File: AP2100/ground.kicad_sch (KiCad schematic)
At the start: 33 parts, among them U21 EMMC04G-M627-A01, U7 LS1043ASE7KQB-Layerscape

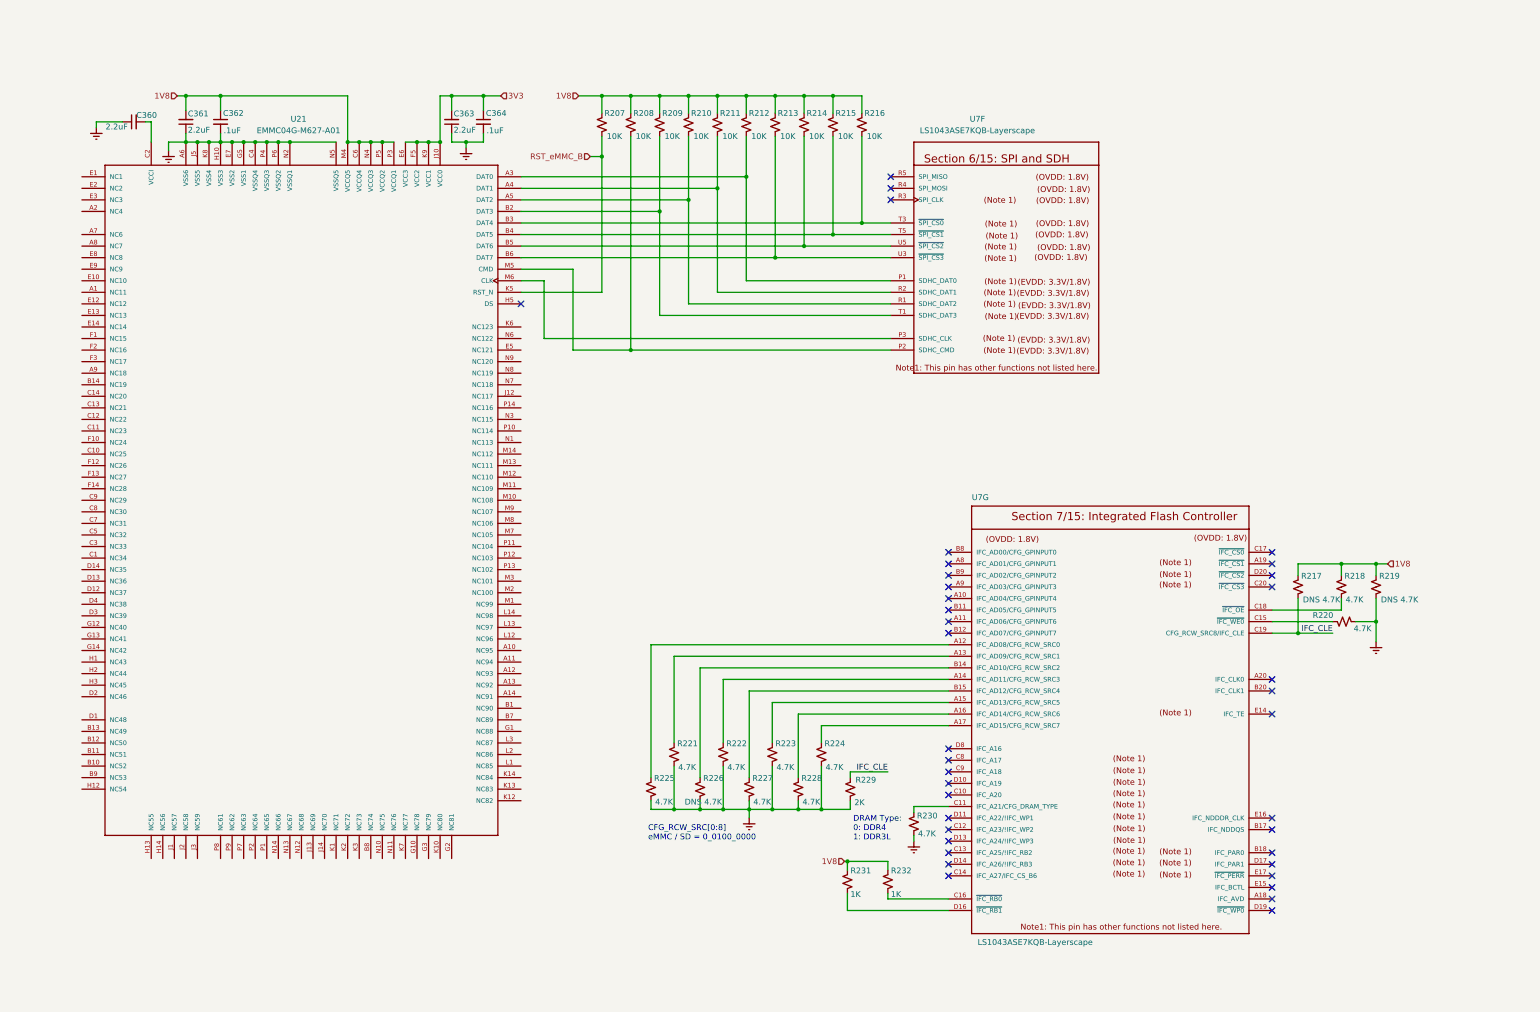
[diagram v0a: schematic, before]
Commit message: Review / cleanup footprints, etc
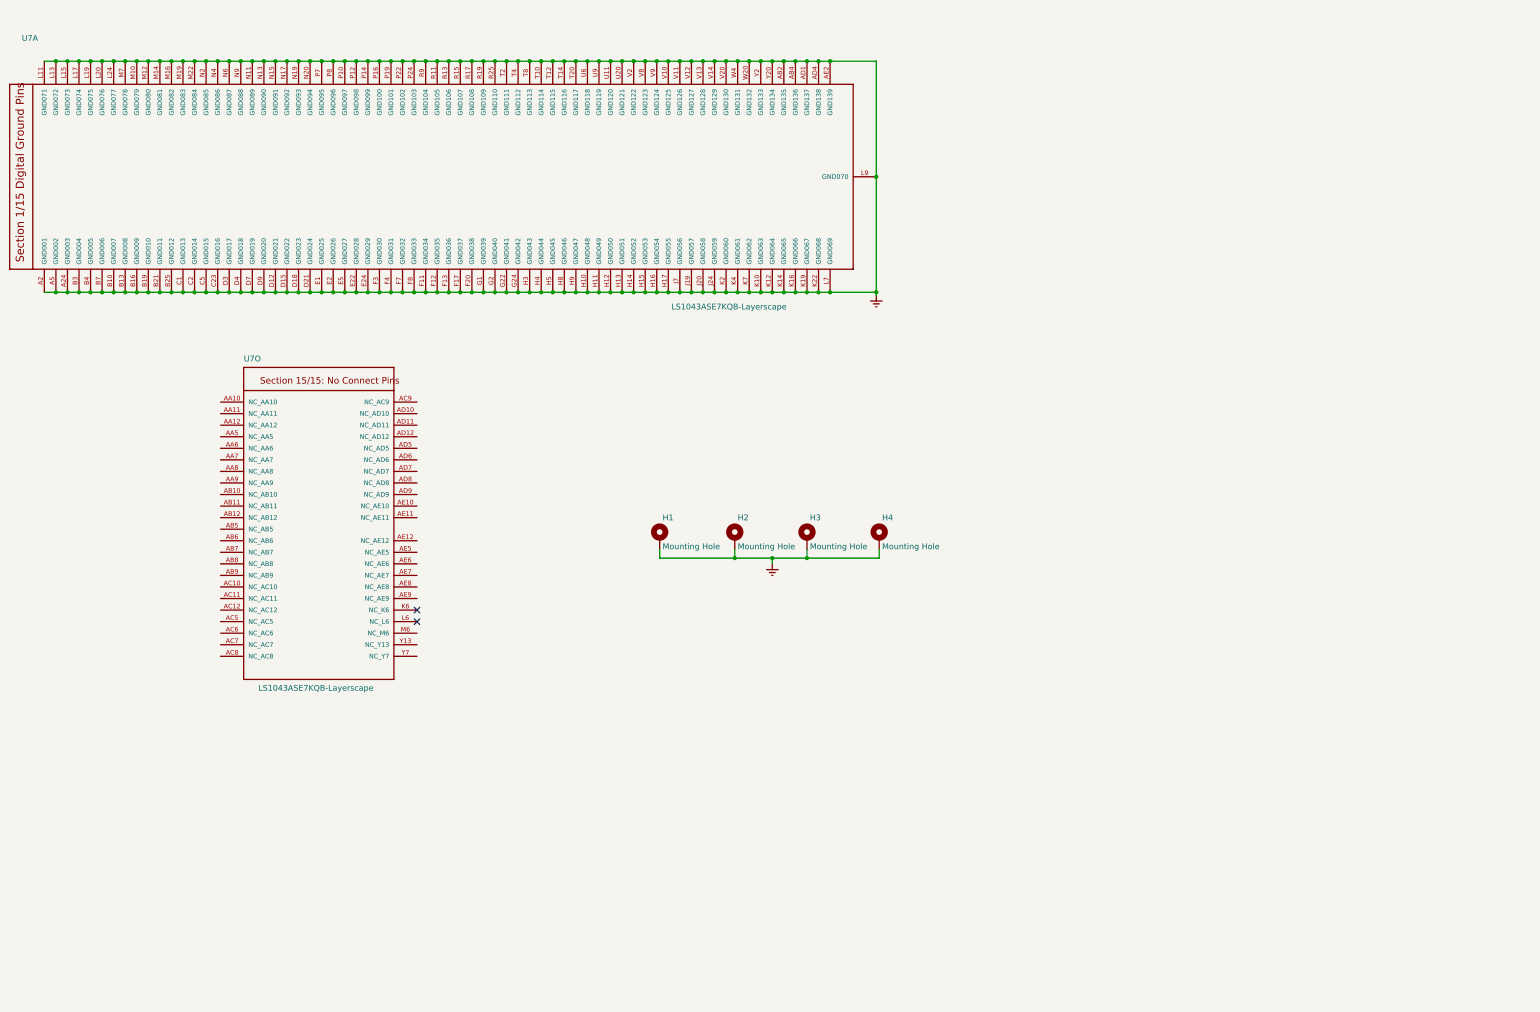
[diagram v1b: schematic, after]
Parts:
- removed C360, C361, C363: 2.2uF, Capacitor_SMD:C_0603_1608Metric, symbol Device:C_Small
- removed C362, C364: .1uF, Capacitor_SMD:C_0402_1005Metric, symbol Device:C_Small
- removed R207, R208, R209, R210, R211, R212, R213, R214, R215, R216: 10K, Resistor_SMD:R_0402_1005Metric, symbol Device:R_Small_US
- removed R217, R219, R226: DNS 4.7K, Resistor_SMD:R_0402_1005Metric, symbol Device:R_Small_US
- removed R218, R220, R221, R222, R223, R224, R225, R227, R228, R230: 4.7K, Resistor_SMD:R_0402_1005Metric, symbol Device:R_Small_US
- removed R229: 2K, Resistor_SMD:R_0402_1005Metric, symbol Device:R_Small_US
- removed R231, R232: 1K, Resistor_SMD:R_0402_1005Metric, symbol Device:R_Small_US
- removed U21: EMMC04G-M627-A01, LIB_EMMC04G-M627:BGA153N50P14X14_1300X1150X100N, symbol EMMC04G-M627-A01:EMMC04G-M627-A01
- removed U7: LS1043ASE7KQB-Layerscape, PLS1043ASE7QQA:BGA621C80P25X25_2100X2100X192N, symbol AP2100-rescue:LS1043ASE7KQB-Layerscape
- added H1, H2, H3, H4: Mounting Hole, MountingHole:MountingHole_2.5mm_Pad_TopBottom, symbol Mechanical:MountingHole_Pad
- added U7: LS1043ASE7KQB-Layerscape, PLS1043ASE7QQA:BGA621C80P25X25_2100X2100X192N, symbol AP2100-rescue:LS1043ASE7KQB-Layerscape
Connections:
- net GND: now also H1.1, H2.1, H3.1, H4.1, U7.A2 (GND001), U7.A24 (GND003), U7.A5 (GND002), U7.AB2 (GND135), U7.AB4 (GND136), U7.AD1 (GND137), U7.AD4 (GND138), U7.AE2 (GND139), U7.B10 (GND007), U7.B13 (GND008), U7.B16 (GND009), U7.B19 (GND010), U7.B21 (GND011), U7.B25 (GND012), U7.B3 (GND004), U7.B4 (GND005), U7.B7 (GND006), U7.C1 (GND013), U7.C2 (GND014), U7.C23 (GND016), U7.C5 (GND015), U7.D12 (GND021), U7.D15 (GND022), U7.D18 (GND023), U7.D21 (GND024), U7.D3 (GND017), U7.D4 (GND018), U7.D7 (GND019), U7.D9 (GND020), U7.E1 (GND025), U7.E2 (GND026), U7.E22 (GND028), U7.E24 (GND029), U7.E5 (GND027), U7.F11 (GND034), U7.F12 (GND035), U7.F13 (GND036), U7.F17 (GND037), U7.F20 (GND038), U7.F3 (GND030), U7.F4 (GND031), U7.F7 (GND032), U7.F8 (GND033), U7.G1 (GND039), U7.G2 (GND040), U7.G22 (GND041), U7.G24 (GND042), U7.H10 (GND048), U7.H11 (GND049), U7.H12 (GND050), U7.H13 (GND051), U7.H14 (GND052), U7.H15 (GND053), U7.H16 (GND054), U7.H17 (GND055), U7.H3 (GND043), U7.H4 (GND044), U7.H5 (GND045), U7.H8 (GND046), U7.H9 (GND047), U7.J19 (GND057), U7.J20 (GND058), U7.J24 (GND059), U7.J7 (GND056), U7.K10 (GND063), U7.K12 (GND064), U7.K14 (GND065), U7.K16 (GND066), U7.K19 (GND067), U7.K2 (GND060), U7.K22 (GND068), U7.K4 (GND061), U7.K7 (GND062), U7.L11 (GND071), U7.L13 (GND072), U7.L15 (GND073), U7.L17 (GND074), U7.L19 (GND075), U7.L20 (GND076), U7.L24 (GND077), U7.L7 (GND069), U7.L9 (GND070), U7.M10 (GND079), U7.M12 (GND080), U7.M14 (GND081), U7.M16 (GND082), U7.M19 (GND083), U7.M22 (GND084), U7.M7 (GND078), U7.N11 (GND089), U7.N13 (GND090), U7.N15 (GND091), U7.N17 (GND092), U7.N19 (GND093), U7.N2 (GND085), U7.N20 (GND094), U7.N4 (GND086), U7.N6 (GND087), U7.N9 (GND088), U7.P10 (GND097), U7.P12 (GND098), U7.P14 (GND099), U7.P16 (GND100), U7.P19 (GND101), U7.P22 (GND102), U7.P24 (GND103), U7.P7 (GND095), U7.P8 (GND096), U7.R11 (GND105), U7.R13 (GND106), U7.R15 (GND107), U7.R17 (GND108), U7.R19 (GND109), U7.R25 (GND110), U7.R9 (GND104), U7.T10 (GND114), U7.T12 (GND115), U7.T14 (GND116), U7.T2 (GND111), U7.T20 (GND117), U7.T4 (GND112), U7.T8 (GND113), U7.U11 (GND120), U7.U20 (GND121), U7.U6 (GND118), U7.U9 (GND119), U7.V10 (GND125), U7.V11 (GND126), U7.V12 (GND127), U7.V13 (GND128), U7.V14 (GND129), U7.V2 (GND122), U7.V20 (GND130), U7.V8 (GND123), U7.V9 (GND124), U7.W20 (GND132), U7.W4 (GND131), U7.Y2 (GND133), U7.Y20 (GND134)
- no-connect marks 38 -> 2
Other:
- note removed: "CFG_RCW_SRC[0:8] eMMC / SD = 0_0100_0000"
- note removed: "DRAM Type: 0: DDR4 1: DDR3L"

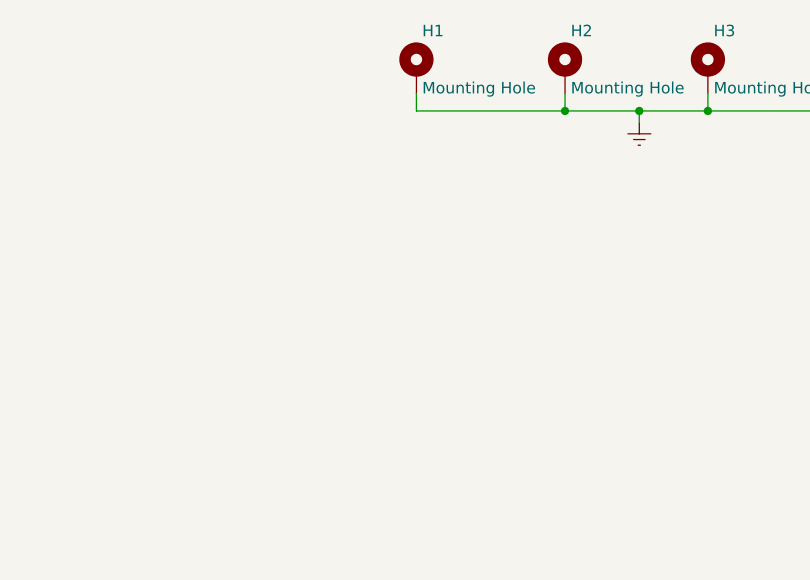
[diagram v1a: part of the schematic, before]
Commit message: Added antenna mounting holes
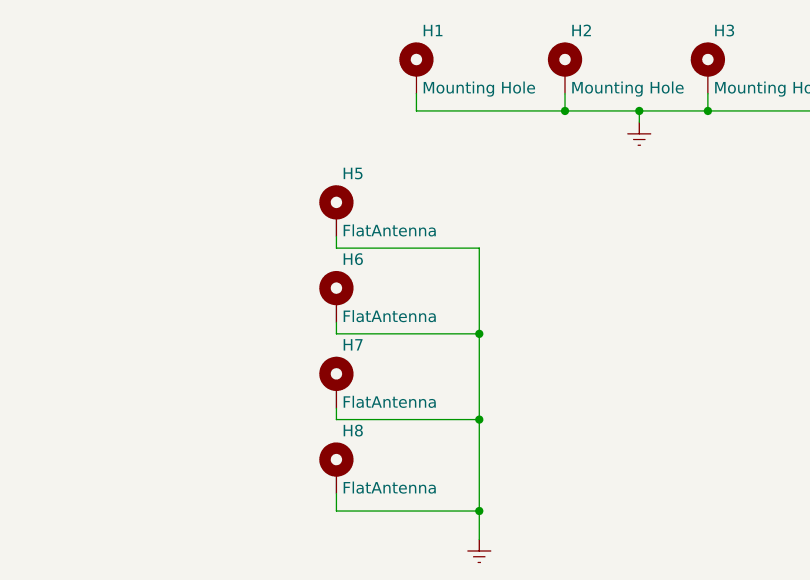
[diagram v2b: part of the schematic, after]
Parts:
- added H5, H6, H7, H8: FlatAntenna, Scott:MountingHole_4.4mm_Pad_TopOnly, symbol Mechanical:MountingHole_Pad
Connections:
- net GND: now also H5.1, H6.1, H7.1, H8.1
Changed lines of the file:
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@@
   (junction (at 187.325 33.02) (diameter 0.9144) (color 0 0 0 0))
   (junction (at 187.325 83.82) (diameter 0.9144) (color 0 0 0 0))
+  (junction (at 187.325 167.005) (diameter 0.9144) (color 0 0 0 0))
+  (junction (at 187.325 176.53) (diameter 0.9144) (color 0 0 0 0))
+  (junction (at 187.325 186.69) (diameter 0.9144) (color 0 0 0 0))
   (junction (at 189.865 33.02) (diameter 0.9144) (color 0 0 0 0))
   (junction (at 189.865 83.82) (diameter 0.9144) (color 0 0 0 0))
@@
     (stroke (width 0) (type solid) (color 0 0 0 0))
   )
+  (wire (pts (xy 171.45 156.21) (xy 171.45 157.48))
+    (stroke (width 0) (type solid) (color 0 0 0 0))
+  )
+  (wire (pts (xy 171.45 157.48) (xy 187.325 157.48))
+    (stroke (width 0) (type solid) (color 0 0 0 0))
+  )
+  (wire (pts (xy 171.45 165.735) (xy 171.45 167.005))
+    (stroke (width 0) (type solid) (color 0 0 0 0))
+  )
+  (wire (pts (xy 171.45 167.005) (xy 187.325 167.005))
+    (stroke (width 0) (type solid) (color 0 0 0 0))
+  )
+  (wire (pts (xy 171.45 175.26) (xy 171.45 176.53))
+    (stroke (width 0) (type solid) (color 0 0 0 0))
+  )
+  (wire (pts (xy 171.45 176.53) (xy 187.325 176.53))
+    (stroke (width 0) (type solid) (color 0 0 0 0))
+  )
+  (wire (pts (xy 171.45 184.785) (xy 171.45 186.69))
+    (stroke (width 0) (type solid) (color 0 0 0 0))
+  )
+  (wire (pts (xy 171.45 186.69) (xy 187.325 186.69))
+    (stroke (width 0) (type solid) (color 0 0 0 0))
+  )
   (wire (pts (xy 172.085 33.02) (xy 174.625 33.02))
     (stroke (width 0) (type solid) (color 0 0 0 0))
@@
     (stroke (width 0) (type solid) (color 0 0 0 0))
   )
+  (wire (pts (xy 187.325 157.48) (xy 187.325 167.005))
+    (stroke (width 0) (type solid) (color 0 0 0 0))
+  )
+  (wire (pts (xy 187.325 167.005) (xy 187.325 176.53))
+    (stroke (width 0) (type solid) (color 0 0 0 0))
+  )
+  (wire (pts (xy 187.325 176.53) (xy 187.325 186.69))
+    (stroke (width 0) (type solid) (color 0 0 0 0))
+  )
+  (wire (pts (xy 187.325 186.69) (xy 187.325 189.865))
+    (stroke (width 0) (type solid) (color 0 0 0 0))
+  )
   (wire (pts (xy 189.865 33.02) (xy 192.405 33.02))
     (stroke (width 0) (type solid) (color 0 0 0 0))
@@
   (wire (pts (xy 228.6 142.24) (xy 228.6 140.335))
     (stroke (width 0) (type solid) (color 0 0 0 0))
+  )
+  (symbol (lib_id "AP2100-rescue:GND-Scott") (at 187.325 189.865 0) (mirror y) (unit 1)
+    (in_bom yes) (on_board yes)
+    (property "Reference" "#PWR0211" (id 0) (at 187.325 196.215 0)
+      (effects (font (size 1.27 1.27)) hide)
+    )
+    (property "Value" "GND" (id 1) (at 187.198 193.6242 0)
+      (effects (font (size 1.27 1.27)) hide)
+    )
+    (property "Footprint" "" (id 2) (at 187.325 189.865 0)
+      (effects (font (size 1.27 1.27)) hide)
+    )
+    (property "Datasheet" "" (id 3) (at 187.325 189.865 0)
+      (effects (font (size 1.27 1.27)) hide)
+    )
   )
   (symbol (lib_id "AP2100-rescue:GND-Scott") (at 205.105 143.51 0) (mirror y) (unit 1)
@@
       (effects (font (size 1.27 1.27)) hide)
     )
+  )
+  (symbol (lib_id "Mechanical:MountingHole_Pad") (at 171.45 153.67 0) (unit 1)
+    (in_bom yes) (on_board yes)
+    (property "Reference" "H5" (id 0) (at 172.085 149.225 0)
+      (effects (font (size 1.27 1.27)) (justify left))
+    )
+    (property "Value" "FlatAntenna" (id 1) (at 172.085 155.575 0)
+      (effects (font (size 1.27 1.27)) (justify left))
+    )
+    (property "Footprint" "Scott:MountingHole_4.4mm_Pad_TopOnly" (id 2) (at 171.45 153.67 0)
+      (effects (font (size 1.27 1.27)) hide)
+    )
+    (property "Datasheet" "~" (id 3) (at 171.45 153.67 0)
+      (effects (font (size 1.27 1.27)) hide)
+    )
+  )
+  (symbol (lib_id "Mechanical:MountingHole_Pad") (at 171.45 163.195 0) (unit 1)
+    (in_bom yes) (on_board yes)
+    (property "Reference" "H6" (id 0) (at 172.085 158.75 0)
+      (effects (font (size 1.27 1.27)) (justify left))
+    )
+    (property "Value" "FlatAntenna" (id 1) (at 172.085 165.1 0)
+      (effects (font (size 1.27 1.27)) (justify left))
+    )
+    (property "Footprint" "Scott:MountingHole_4.4mm_Pad_TopOnly" (id 2) (at 171.45 163.195 0)
+      (effects (font (size 1.27 1.27)) hide)
+    )
+    (property "Datasheet" "~" (id 3) (at 171.45 163.195 0)
+      (effects (font (size 1.27 1.27)) hide)
+    )
+  )
+  (symbol (lib_id "Mechanical:MountingHole_Pad") (at 171.45 172.72 0) (unit 1)
+    (in_bom yes) (on_board yes)
+    (property "Reference" "H7" (id 0) (at 172.085 168.275 0)
+      (effects (font (size 1.27 1.27)) (justify left))
+    )
+    (property "Value" "FlatAntenna" (id 1) (at 172.085 174.625 0)
+      (effects (font (size 1.27 1.27)) (justify left))
+    )
+    (property "Footprint" "Scott:MountingHole_4.4mm_Pad_TopOnly" (id 2) (at 171.45 172.72 0)
+      (effects (font (size 1.27 1.27)) hide)
+    )
+    (property "Datasheet" "~" (id 3) (at 171.45 172.72 0)
+      (effects (font (size 1.27 1.27)) hide)
+    )
+  )
+  (symbol (lib_id "Mechanical:MountingHole_Pad") (at 171.45 182.245 0) (unit 1)
+    (in_bom yes) (on_board yes)
+    (property "Reference" "H8" (id 0) (at 172.085 177.8 0)
+      (effects (font (size 1.27 1.27)) (justify left))
+    )
+    (property "Value" "FlatAntenna" (id 1) (at 172.085 184.15 0)
+      (effects (font (size 1.27 1.27)) (justify left))
+    )
+    (property "Footprint" "Scott:MountingHole_4.4mm_Pad_TopOnly" (id 2) (at 171.45 182.245 0)
+      (effects (font (size 1.27 1.27)) hide)
+    )
+    (property "Datasheet" "~" (id 3) (at 171.45 182.245 0)
+      (effects (font (size 1.27 1.27)) hide)
+    )

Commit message: Not sure
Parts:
- U7: value LS1043ASE7KQB-Layerscape -> LS1043ASE7xxx; PartsBoxID (none) -> LS1043ASE7
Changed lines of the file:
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@@
   (junction (at 227.965 58.42) (diameter 0.9144) (color 0 0 0 0))
   (junction (at 227.965 83.82) (diameter 0.9144) (color 0 0 0 0))
+  (no_connect (at 127 156.21))
   (no_connect (at 127 153.67))
-  (no_connect (at 127 156.21))
   (wire (pts (xy 45.085 33.02) (xy 47.625 33.02))
     (stroke (width 0) (type solid) (color 0 0 0 0))
@@
     (in_bom yes) (on_board yes)
     (property "Reference" "U7" (id 0) (at 90.805 98.425 0))
-    (property "Value" "LS1043ASE7KQB-Layerscape" (id 1) (at 104.775 170.815 0))
+    (property "Value" "LS1043ASE7xxx" (id 1) (at 104.775 170.815 0))
     (property "Footprint" "PLS1043ASE7QQA:BGA621C80P25X25_2100X2100X192N" (id 2) (at 104.14 133.35 0)
       (effects (font (size 1.27 1.27)) hide)
@@
       (effects (font (size 1.27 1.27)) hide)
     )
+    (property "PartsBoxID" "LS1043ASE7" (id 4) (at 104.14 133.35 0)
+      (effects (font (size 1.27 1.27)) hide)
+    )
   )
   (symbol (lib_id "AP2100-rescue:LS1043ASE7KQB-Layerscape") (at 128.905 58.42 90) (unit 1)
     (in_bom yes) (on_board yes)
     (property "Reference" "U7" (id 0) (at 41.91 27.94 90))
-    (property "Value" "LS1043ASE7KQB-Layerscape" (id 1) (at 195.58 86.995 90))
+    (property "Value" "LS1043ASE7xxx" (id 1) (at 195.58 86.995 90))
     (property "Footprint" "PLS1043ASE7QQA:BGA621C80P25X25_2100X2100X192N" (id 2) (at 128.905 58.42 0)
       (effects (font (size 1.27 1.27)) hide)
@@
       (effects (font (size 1.27 1.27)) hide)
     )
+    (property "PartsBoxID" "LS1043ASE7" (id 4) (at 128.905 58.42 0)
+      (effects (font (size 1.27 1.27)) hide)
+    )
